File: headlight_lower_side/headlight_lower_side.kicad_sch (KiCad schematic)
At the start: 21 parts, among them J1 Conn_01x06_Pin, J2 Conn_02x03_Odd_Even

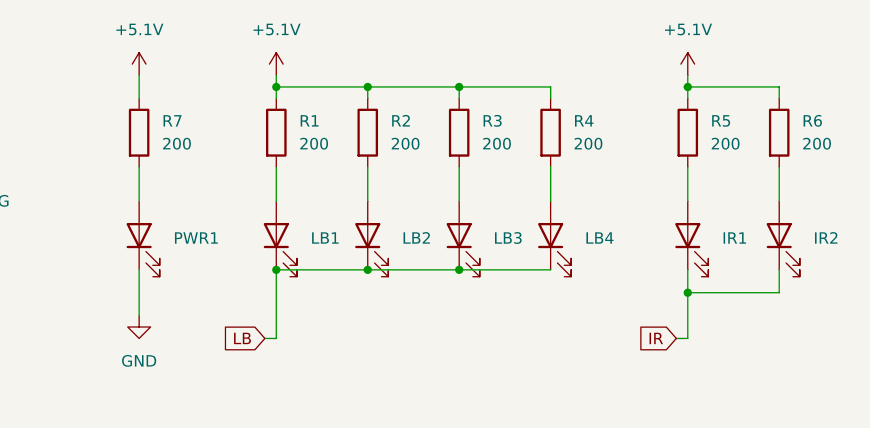
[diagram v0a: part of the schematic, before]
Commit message: 基板防水REV00発注完了
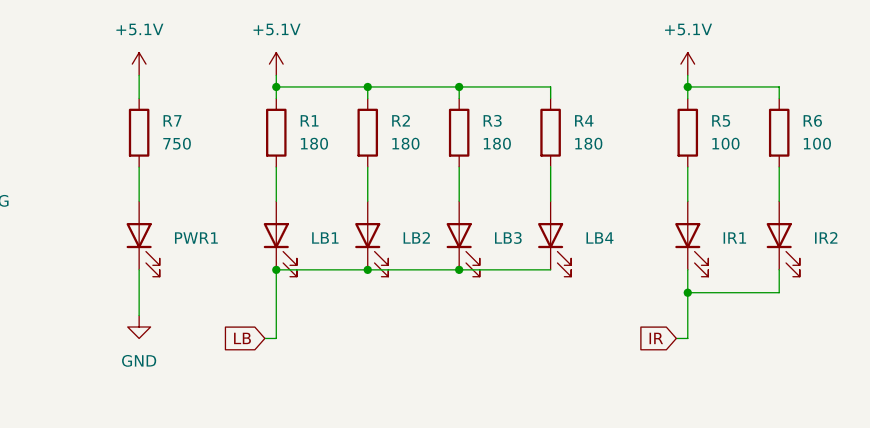
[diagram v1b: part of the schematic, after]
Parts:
- R1, R2, R3, R4: value 200 -> 180
- R5, R6: value 200 -> 100
- R7: value 200 -> 750
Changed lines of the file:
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@@
 			)
 		)
-		(property "Value" "200"
+		(property "Value" "180"
 			(at 144.78 30.4799 0)
 			(effects
@@
 			)
 		)
-		(property "Value" "200"
+		(property "Value" "100"
 			(at 180.34 30.4799 0)
 			(effects
@@
 			)
 		)
-		(property "Value" "200"
+		(property "Value" "100"
 			(at 170.18 30.4799 0)
 			(effects
@@
 			)
 		)
-		(property "Value" "200"
+		(property "Value" "180"
 			(at 124.46 30.4799 0)
 			(effects
@@
 			)
 		)
-		(property "Value" "200"
+		(property "Value" "180"
 			(at 154.94 30.4799 0)
 			(effects
@@
 			)
 		)
-		(property "Value" "200"
+		(property "Value" "750"
 			(at 109.22 30.4799 0)
 			(effects
@@
 			)
 		)
-		(property "Value" "200"
+		(property "Value" "180"
 			(at 134.62 30.4799 0)
 			(effects
